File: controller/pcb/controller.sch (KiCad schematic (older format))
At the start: 71 parts, among them J1 POWER, J2 10K POT, Q1 2N2222, Q10 2N2222, Q11 2N2222, Q12 TIP41, Q13 TIP41, Q14 2N2907, Q15 2N2222, Q2 TIP42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

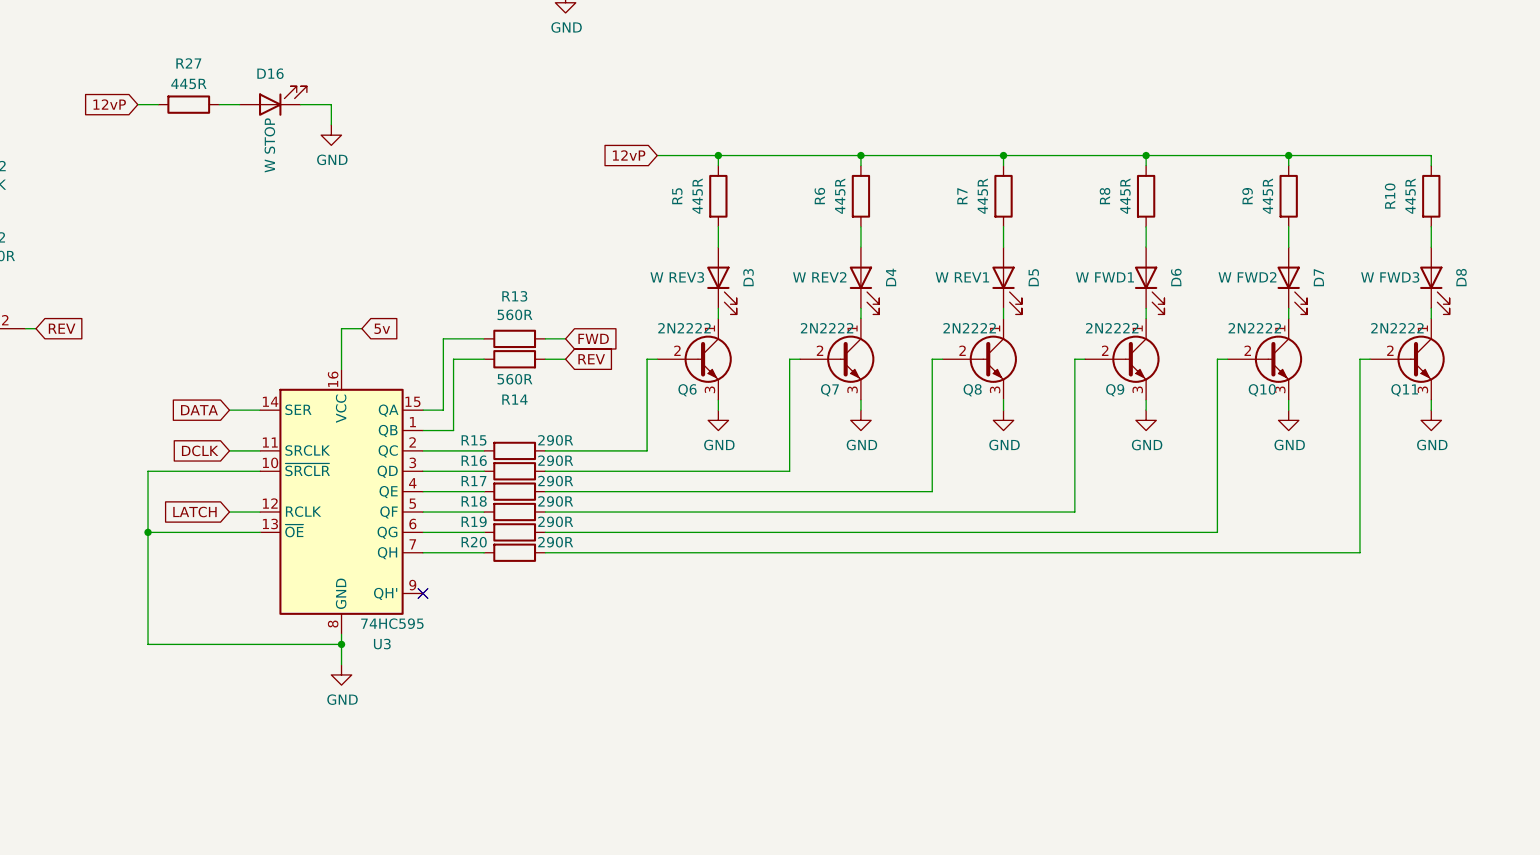
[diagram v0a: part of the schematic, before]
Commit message: Added .gitignore. Further work on controller firmware.
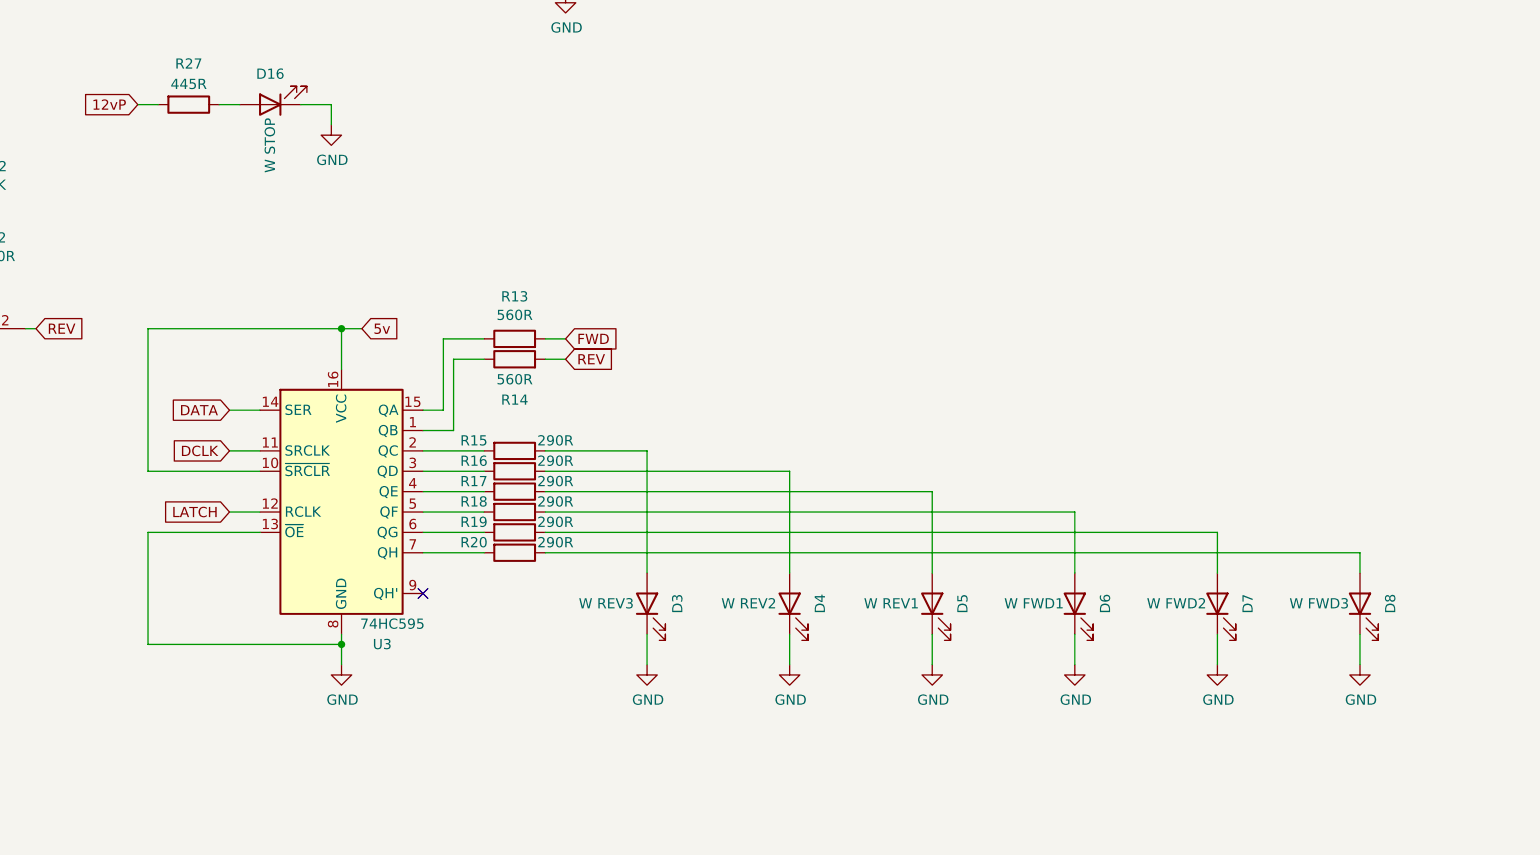
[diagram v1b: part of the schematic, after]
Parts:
- removed Q10, Q11, Q6, Q7, Q8, Q9: 2N2222, TO_SOT_Packages_THT:TO-92_Inline_Wide, symbol Transistor_BJT:BC237
- removed R10, R5, R6, R7, R8, R9: 445R, Resistors_THT:R_Axial_DIN0411_L9.9mm_D3.6mm_P12.70mm_Horizontal, symbol Device:R
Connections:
- net 5v: now also U3.10 (~SRCLR)
- net GND: now also D3.1 (K), D4.1 (K), D5.1 (K), D6.1 (K), D7.1 (K), D8.1 (K); no longer U3.10 (~SRCLR)
- net at D3.2 (A): now also R15.1
- net at D4.2 (A): now also R16.1
- net at D5.2 (A): now also R17.1
- net at D7.2 (A): now also R19.1
- net at D6.2 (A): now also R18.1
- net at R20.1: now also D8.2 (A)
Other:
- moved on the sheet: D3, D4, D5, D6, D7, D8

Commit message: Further firmware tweaks.
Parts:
- added D? (x4): 1N4001, symbol Device:D
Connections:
- net 12vP: now also D?.1 (K), D?.1 (K)
- net FWD: now also R14.2; no longer R13.2
- net GND: now also D?.2 (A), D?.2 (A)
- net REV: now also R13.2; no longer R14.2
- net TRACK+: now also D?.1 (K), D?.2 (A)
- net TRACK-: now also D?.1 (K), D?.2 (A)
- net at R15.2: now also U3.15 (QA); no longer U3.2 (QC)
- net at R16.2: now also U3.1 (QB); no longer U3.3 (QD)
- net at R17.2: now also U3.2 (QC); no longer U3.4 (QE)
- net at R14.1: now also U3.4 (QE); no longer U3.1 (QB)
- net at R13.1: now also U3.3 (QD); no longer U3.15 (QA)
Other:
- moved on the sheet: R13, R14, R15, R16, R17
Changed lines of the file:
@@
 	1    0    0    -1
 $EndComp
-Text GLabel 6350 4000 2    50   Input ~ 0
+Text GLabel 6350 4750 2    50   Input ~ 0
 FWD
-Text GLabel 6350 4100 2    50   Input ~ 0
+Text GLabel 6350 4650 2    50   Input ~ 0
 REV
 $Comp
@@
 L Device:R R14
 U 1 1 5EF1835E
-P 6100 4100
-F 0 "R14" V 5900 4100 50  0000 C CNN
-F 1 "560R" V 6000 4100 50  0000 C CNN
-F 2 "Resistors_THT:R_Axial_DIN0411_L9.9mm_D3.6mm_P12.70mm_Horizontal" V 6030 4100 50  0001 C CNN
-F 3 "~" H 6100 4100 50  0001 C CNN
-	1    6100 4100
+P 6100 4750
+F 0 "R14" V 5900 4750 50  0000 C CNN
+F 1 "560R" V 6000 4750 50  0000 C CNN
+F 2 "Resistors_THT:R_Axial_DIN0411_L9.9mm_D3.6mm_P12.70mm_Horizontal" V 6030 4750 50  0001 C CNN
+F 3 "~" H 6100 4750 50  0001 C CNN
+	1    6100 4750
 	0    -1   -1   0
 $EndComp
@@
 L Device:R R13
 U 1 1 5EF1860D
-P 6100 4000
-F 0 "R13" V 6307 4000 50  0000 C CNN
-F 1 "560R" V 6216 4000 50  0000 C CNN
-F 2 "Resistors_THT:R_Axial_DIN0411_L9.9mm_D3.6mm_P12.70mm_Horizontal" V 6030 4000 50  0001 C CNN
-F 3 "~" H 6100 4000 50  0001 C CNN
-	1    6100 4000
+P 6100 4650
+F 0 "R13" V 6307 4650 50  0000 C CNN
+F 1 "560R" V 6216 4650 50  0000 C CNN
+F 2 "Resistors_THT:R_Axial_DIN0411_L9.9mm_D3.6mm_P12.70mm_Horizontal" V 6030 4650 50  0001 C CNN
+F 3 "~" H 6100 4650 50  0001 C CNN
+	1    6100 4650
 	0    -1   -1   0
 $EndComp
@@
 	5250 5450 5250 5500
 Wire Wire Line
-	6350 4000 6250 4000
-Wire Wire Line
-	6250 4100 6350 4100
-Wire Wire Line
-	5950 4000 5750 4000
-Wire Wire Line
-	5750 4000 5750 4350
-Wire Wire Line
-	5750 4350 5650 4350
-Wire Wire Line
-	5950 4100 5800 4100
-Wire Wire Line
-	5800 4100 5800 4450
-Wire Wire Line
-	5800 4450 5650 4450
+	6350 4650 6250 4650
+Wire Wire Line
+	6250 4750 6350 4750
 Text GLabel 4700 4350 0    50   Input ~ 0
 DATA
@@
 L Device:R R15
 U 1 1 5ECDE1CF
-P 6100 4550
-F 0 "R15" V 6050 4350 50  0000 C CNN
-F 1 "290R" V 6050 4750 50  0000 C CNN
-F 2 "Resistors_THT:R_Axial_DIN0411_L9.9mm_D3.6mm_P12.70mm_Horizontal" V 6030 4550 50  0001 C CNN
-F 3 "~" H 6100 4550 50  0001 C CNN
-	1    6100 4550
-	0    1    1    0
-$EndComp
-Wire Wire Line
-	5650 4550 5950 4550
-Wire Wire Line
-	6250 4550 6750 4550
+P 6100 4350
+F 0 "R15" V 6050 4150 50  0000 C CNN
+F 1 "290R" V 6050 4550 50  0000 C CNN
+F 2 "Resistors_THT:R_Axial_DIN0411_L9.9mm_D3.6mm_P12.70mm_Horizontal" V 6030 4350 50  0001 C CNN
+F 3 "~" H 6100 4350 50  0001 C CNN
+	1    6100 4350
+	0    1    1    0
+$EndComp
+Wire Wire Line
+	6250 4350 6750 4350
 $Comp
 L Device:LED D3
@@
 L Device:R R16
 U 1 1 5ED4926F
-P 6100 4650
-F 0 "R16" V 6050 4450 50  0000 C CNN
-F 1 "290R" V 6050 4850 50  0000 C CNN
-F 2 "Resistors_THT:R_Axial_DIN0411_L9.9mm_D3.6mm_P12.70mm_Horizontal" V 6030 4650 50  0001 C CNN
-F 3 "~" H 6100 4650 50  0001 C CNN
-	1    6100 4650
+P 6100 4450
+F 0 "R16" V 6050 4250 50  0000 C CNN
+F 1 "290R" V 6050 4650 50  0000 C CNN
+F 2 "Resistors_THT:R_Axial_DIN0411_L9.9mm_D3.6mm_P12.70mm_Horizontal" V 6030 4450 50  0001 C CNN
+F 3 "~" H 6100 4450 50  0001 C CNN
+	1    6100 4450
 	0    1    1    0
 $EndComp
@@
 L Device:R R17
 U 1 1 5ED49375
-P 6100 4750
-F 0 "R17" V 6050 4550 50  0000 C CNN
-F 1 "290R" V 6050 4950 50  0000 C CNN
-F 2 "Resistors_THT:R_Axial_DIN0411_L9.9mm_D3.6mm_P12.70mm_Horizontal" V 6030 4750 50  0001 C CNN
-F 3 "~" H 6100 4750 50  0001 C CNN
-	1    6100 4750
+P 6100 4550
+F 0 "R17" V 6050 4350 50  0000 C CNN
+F 1 "290R" V 6050 4750 50  0000 C CNN
+F 2 "Resistors_THT:R_Axial_DIN0411_L9.9mm_D3.6mm_P12.70mm_Horizontal" V 6030 4550 50  0001 C CNN
+F 3 "~" H 6100 4550 50  0001 C CNN
+	1    6100 4550
 	0    1    1    0
 $EndComp
@@
 $EndComp
 Wire Wire Line
-	5650 4650 5950 4650
-Wire Wire Line
-	5650 4750 5950 4750
-Wire Wire Line
 	5650 4850 5950 4850
 Wire Wire Line
@@
 	5650 5050 5950 5050
 Wire Wire Line
-	6250 4650 7450 4650
-Wire Wire Line
-	6250 4750 8150 4750
+	6250 4450 7450 4450
+Wire Wire Line
+	6250 4550 8150 4550
 Wire Wire Line
 	6250 4850 8850 4850
@@
 	8850 4850 8850 5150
 Wire Wire Line
-	8150 4750 8150 5150
-Wire Wire Line
-	7450 4650 7450 5150
-Wire Wire Line
-	6750 4550 6750 5150
+	8150 4550 8150 5150
+Wire Wire Line
+	7450 4450 7450 5150
+Wire Wire Line
+	6750 4350 6750 5150
+$Comp
+L Device:D D?
+U 1 1 5EF8C3FB
+P 9250 3350
+F 0 "D?" V 9204 3430 50  0000 L CNN
+F 1 "1N4001" V 9250 2950 50  0000 L CNN
+F 2 "" H 9250 3350 50  0001 C CNN
+F 3 "~" H 9250 3350 50  0001 C CNN
+	1    9250 3350
+	0    1    1    0
+$EndComp
+Text GLabel 9000 3000 0    50   Input ~ 0
+12vP
+Text GLabel 9050 3600 0    50   Input ~ 0
+TRACK+
+Text GLabel 9750 3600 2    50   Input ~ 0
+TRACK-
+$Comp
+L Device:D D?
+U 1 1 5EF8DBEF
+P 9250 3850
+F 0 "D?" V 9204 3930 50  0000 L CNN
+F 1 "1N4001" V 9300 3450 50  0000 L CNN
+F 2 "" H 9250 3850 50  0001 C CNN
+F 3 "~" H 9250 3850 50  0001 C CNN
+	1    9250 3850
+	0    1    1    0
+$EndComp
+$Comp
+L Device:D D?
+U 1 1 5EF8DD5D
+P 9550 3350
+F 0 "D?" V 9504 3430 50  0000 L CNN
+F 1 "1N4001" V 9595 3430 50  0000 L CNN
+F 2 "" H 9550 3350 50  0001 C CNN
+F 3 "~" H 9550 3350 50  0001 C CNN
+	1    9550 3350
+	0    1    1    0
+$EndComp
+$Comp
+L Device:D D?
+U 1 1 5EF8DE71
+P 9550 3850
+F 0 "D?" V 9504 3930 50  0000 L CNN
+F 1 "1N4001" V 9595 3930 50  0000 L CNN
+F 2 "" H 9550 3850 50  0001 C CNN
+F 3 "~" H 9550 3850 50  0001 C CNN
+	1    9550 3850
+	0    1    1    0
+$EndComp
+Wire Wire Line
+	9000 3000 9250 3000
+Wire Wire Line
+	9250 3000 9250 3200
+Wire Wire Line
+	9250 3000 9550 3000
+Wire Wire Line
+	9550 3000 9550 3200
+Wire Wire Line
+	9250 3500 9250 3600
+Wire Wire Line
+	9550 3500 9550 3600
+Wire Wire Line
+	9250 4000 9250 4250
+Wire Wire Line
+	9550 4000 9550 4250
+Wire Wire Line
+	9550 4250 9400 4250
+Wire Wire Line
+	9050 3600 9250 3600
+Connection ~ 9250 3600
+Wire Wire Line
+	9250 3600 9250 3700
+Wire Wire Line
+	9750 3600 9550 3600
+Connection ~ 9550 3600
+Wire Wire Line
+	9550 3600 9550 3700
+$Comp
+L power:GND #PWR?
+U 1 1 5EFD4272
+P 9400 4350
+F 0 "#PWR?" H 9400 4100 50  0001 C CNN
+F 1 "GND" H 9405 4177 50  0000 C CNN
+F 2 "" H 9400 4350 50  0001 C CNN
+F 3 "" H 9400 4350 50  0001 C CNN
+	1    9400 4350
+	1    0    0    -1
+$EndComp
+Connection ~ 9250 3000
+Wire Wire Line
+	9400 4350 9400 4250
+Connection ~ 9400 4250
+Wire Wire Line
+	9400 4250 9250 4250
+Wire Wire Line
+	5650 4350 5950 4350
+Wire Wire Line
+	5650 4450 5950 4450
+Wire Wire Line
+	5650 4550 5950 4550
+Wire Wire Line
+	5650 4650 5950 4650
+Wire Wire Line
+	5650 4750 5950 4750
 $EndSCHEMATC

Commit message: Updates
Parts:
- removed D1: 1N5400, Diodes_THT:D_DO-15_P15.24mm_Horizontal, symbol Device:D
- removed D11, D13, D14: R OL, LEDs:LED_D5.0mm, symbol Device:LED
- removed D9: 5.1V, Diodes_THT:D_DO-41_SOD81_P7.62mm_Horizontal, symbol Device:D_Zener
- removed Q14: 2N2907, TO_SOT_Packages_THT:TO-92_Inline_Wide, symbol Transistor_BJT:BC559
- removed R24: 1K, Resistors_THT:R_Axial_DIN0411_L9.9mm_D3.6mm_P12.70mm_Horizontal, symbol Device:R
- removed R26: 240R, Resistors_THT:R_Axial_DIN0411_L9.9mm_D3.6mm_P12.70mm_Horizontal, symbol Device:R
- removed RV1, RV2: 10K, carnivalben:TrimPot_RM065, symbol Device:R_POT_TRIM
- added R? (x2): 100K, Resistors_THT:R_Axial_DIN0411_L9.9mm_D3.6mm_P12.70mm_Horizontal, symbol Device:R
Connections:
- net 12vP is gone; now on net +12V: C1.1, C2.1, D10.2 (A), D?.1 (K), D?.1 (K), Q2.3 (E), Q3.3 (E), R1.2, R27.2, U1.1 (VI)
- net at Q4.1 (C): now also Q2.1 (B), R?.1; no longer R11.1
- net at Q4.3 (E): now also R11.2; no longer Q13.1 (B)
- net at Q5.1 (C): now also Q3.1 (B), R?.1; no longer R12.1
- net at Q5.3 (E): now also R12.2; no longer Q12.1 (B)
- net 12v renamed +12V
- net +12V: now also R?.2, R?.2
- new net: Q12.1 (B), R12.1
- new net: Q13.1 (B), R11.1
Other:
- moved on the sheet: Q4, Q5, R11, R12
